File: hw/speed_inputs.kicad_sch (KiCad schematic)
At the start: 21 parts, among them U701 TLV3201

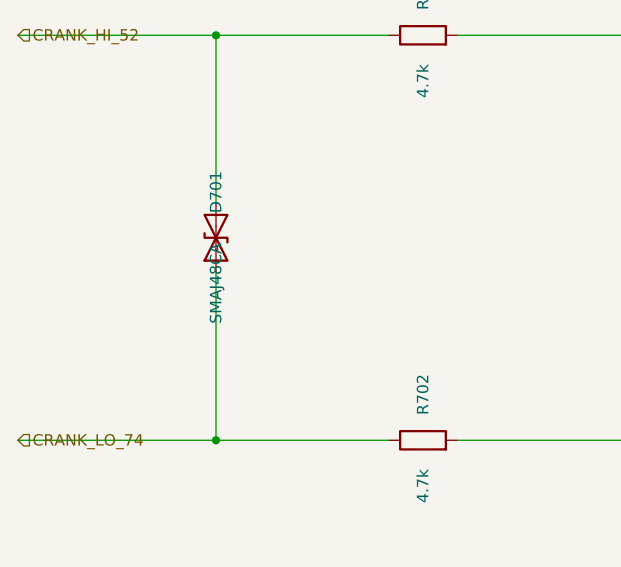
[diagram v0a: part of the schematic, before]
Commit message: Choose the diodes; the boost VDD clamp was 10 V over its pin rating
Part numbers for 27 diodes, each against a retrieved datasheet, applied
through one table (schlib.CHOSEN) keyed by symbol and class value, so
the class stays on the part as a field:
  VS-16EDH02HM3 x7   injector recirculation / blocking / freewheel
  VS-2EMH02HM3       boost diode
  VS-1EMH02HM3 x8    bootstrap and relay flyback
  VS-3ECH02HM3       metering freewheel
  SS20PH102HM3       negative-clamp backstop Schottky
  SMCJ43CA-HM3, SMAJ48CA-HE3, BZX84-C12-Q x2, BZX84-C13-Q, BZG03C36-HM3

The TPS40210 VDD clamp had been checked as an ideal 43.0 V source
behind 47 ohm. The real part in that class (40-46 V, +0.12 %/K, 45 ohm)
puts 61.9 V on a 52 V pin at 125 C, and its 40 V minimum conducts on
the load dump it was chosen to avoid. Now 220 ohm -- which the chosen
switch's gate charge allows -- and a 36 V zener: 46.6 V worst case with
tolerance, tempco and impedance, 33 mA on the dump. 39 V was tried
first; the transient_clamp rail table rejected it at 1.05x. The old
design stays as a pinned check.

TO-277A and SOT-23 zeners put the cathode on pad 3. gen_footprints.py
derives renumbered copies into lib/ecu25kva.pretty (new fp-lib-table).
The GATE_KILL zener, footprinted in the previous commit with the stock
SOT-23, had been reversed.

Left open as LOWV-CLAMP: the 15 zeners at 3.0 and 3.3 V. At tens of uA
a sub-5 V zener's knee is soft -- the datasheet allows 10 uA at 1 V --
and the model's sharp-knee zener hides it.

24/24 sim blocks, netlist gate passing, 74 of 297 parts with footprints.
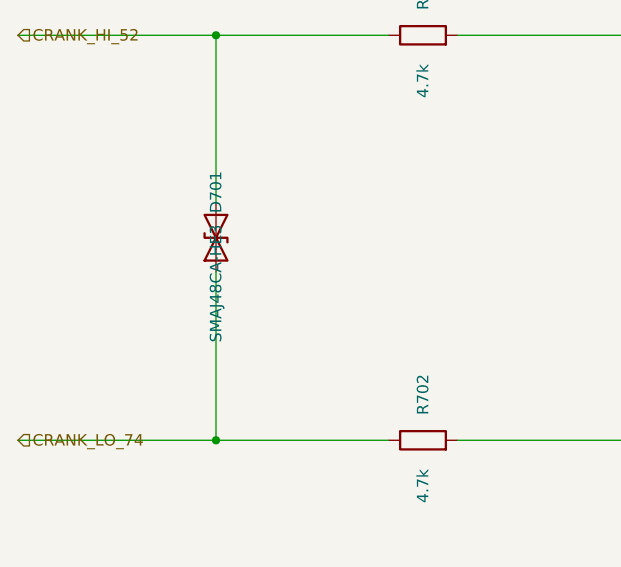
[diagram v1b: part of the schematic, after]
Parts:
- D701: value SMAJ48CA -> SMAJ48CA-HE3; footprint (none) -> Diode_SMD:D_SMA; Chosen (none) -> Vishay TransZorb, 48 V standoff, VBR 53.3-58.9 V, 400 W, AE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; Class (none) -> SMAJ48CA; MPN (none) -> SMAJ48CA-HE3
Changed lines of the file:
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@@
       (effects (font (size 1.27 1.27)))
     )
-    (property "Value" "SMAJ48CA" (id 1) (at 62.0 97.58 0)
+    (property "Value" "SMAJ48CA-HE3" (id 1) (at 62.0 97.58 0)
       (effects (font (size 1.27 1.27)))
     )
-    (property "Footprint" "" (id 2) (at 62.0 92.5 0)
+    (property "Footprint" "Diode_SMD:D_SMA" (id 2) (at 62.0 92.5 0)
       (effects (font (size 1.27 1.27)) hide)
     )
@@
       (effects (font (size 1.27 1.27)) hide)
     )
-    (property "Tag" "VR-CLAMP" (id 4) (at 62.0 92.5 0)
+    (property "MPN" "SMAJ48CA-HE3" (id 4) (at 62.0 92.5 0)
       (effects (font (size 1.27 1.27)) hide)
     )
-    (property "Note" "Bidirectional, across the pair. Standoff has to clear the signal itself: VR amplitude is proportional to speed, about 20 V peak at 1500 rpm, so a part that clamps at 24 V would clip a runaway engine's own crank signal -- the one time the ECU most needs to keep counting teeth. 48 V clears 3600 rpm." (id 5) (at 62.0 92.5 0)
+    (property "Class" "SMAJ48CA" (id 5) (at 62.0 92.5 0)
       (effects (font (size 1.27 1.27)) hide)
     )
+    (property "Chosen" "Vishay TransZorb, 48 V standoff, VBR 53.3-58.9 V, 400 W, AEC-Q101" (id 6) (at 62.0 92.5 0)
+      (effects (font (size 1.27 1.27)) hide)
+    )
+    (property "Tag" "VR-CLAMP" (id 7) (at 62.0 92.5 0)
+      (effects (font (size 1.27 1.27)) hide)
+    )
+    (property "Note" "Bidirectional, across the pair. Standoff has to clear the signal itself: VR amplitude is proportional to speed, about 20 V peak at 1500 rpm, so a part that clamps at 24 V would clip a runaway engine's own crank signal -- the one time the ECU most needs to keep counting teeth. 48 V clears 3600 rpm." (id 8) (at 62.0 92.5 0)
+      (effects (font (size 1.27 1.27)) hide)
+    )

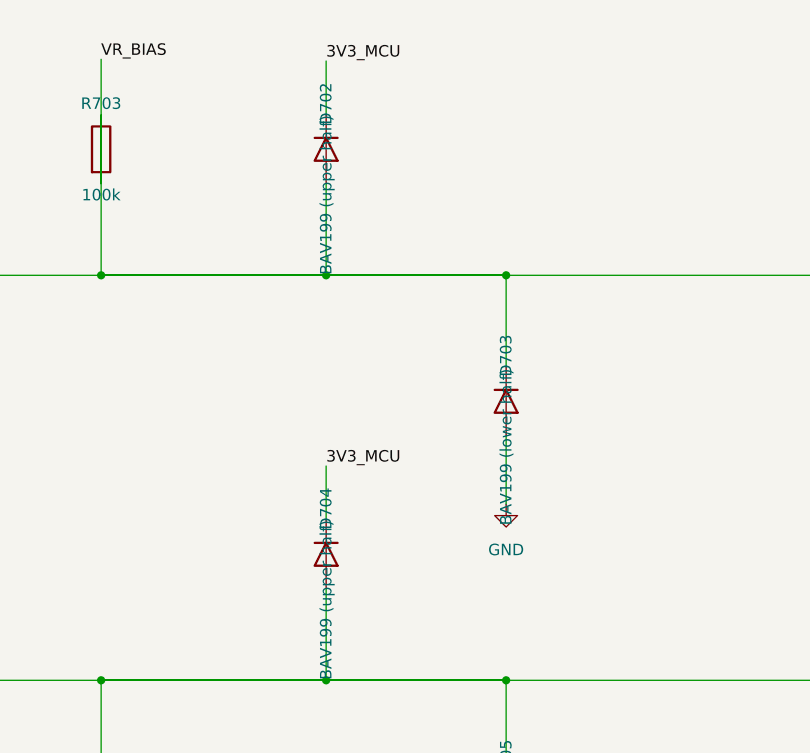
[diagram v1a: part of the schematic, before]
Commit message: Package every resistor and capacitor from the voltage across it
hw/assign_passives.py sizes all 188 chip R and C from a per-net table
of continuous and peak voltage (73.3 V pulse 2a, 104 V boost, bootstrap
domains riding on the bank nodes), against Vishay CRCW e3 resistor
ratings (Umax with 1.09x margin, power derated to 0.588x at a 105 C
board) and KEMET's automotive X7R waterfall (parsed by x-coordinate;
the text layout misreads its columns). schlib.place() applies the map
by ref and value; check_netlist fails on any unpackaged R or C.

Found along the way:
- 4.7 uF at 100 V is not in automotive X7R. The EMI filter C1, buck
  input and boost input are now 2 x 2.2 uF 100 V 1210; emi_filter.cir
  models the pair and its cold corner was re-pinned (0.6 dB worse).
- The twelve 470 ohm gate pulldowns need 2010: 0.31 W each at 100%
  duty. Recorded; 1k may now be possible against the real Crss.
- Local labels at 180 degrees were justified in the wrong frame on
  every sheet -- the bug fixed for hierarchical labels earlier -- so
  their text sat across their own wire. Fixed in schlib.label().

Internal nodes whose voltage matters now carry names (FB_BOOST_MID,
CAN1_SPLIT, ...); auto-names like Net-(R407-Pad2) move when parts are
added ahead of them.

24/24 sim blocks, netlist gate passing, 264 of 302 parts footprinted.
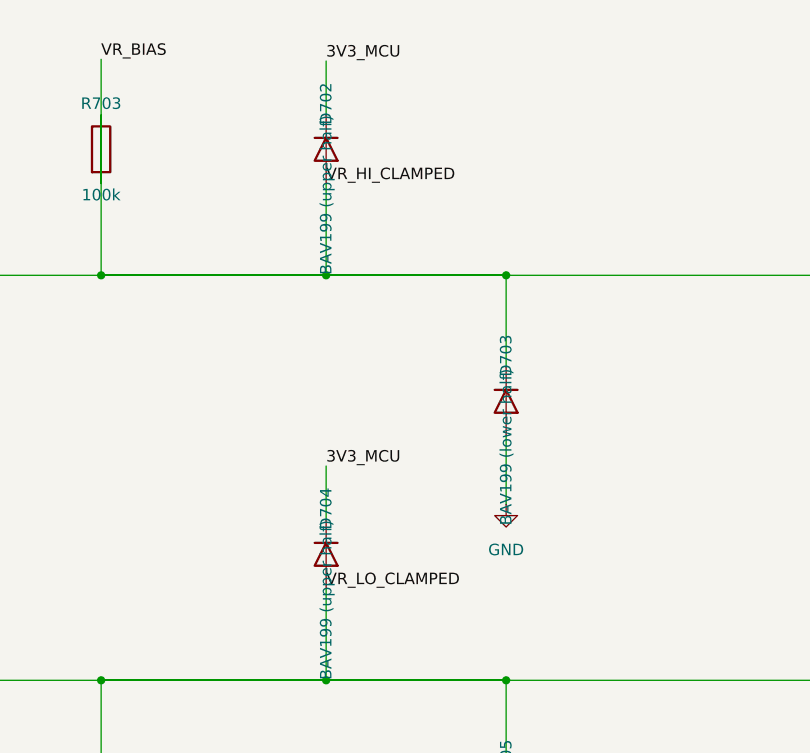
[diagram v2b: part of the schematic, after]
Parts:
- C701, C702, C703, C705: footprint (none) -> Capacitor_SMD:C_0603_1608Metric
- C704: footprint (none) -> Capacitor_SMD:C_0805_2012Metric
- R701, R702, R703, R704, R705, R706, R707, R708, R709: footprint (none) -> Resistor_SMD:R_0603_1608Metric
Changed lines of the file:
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@@
       (effects (font (size 1.27 1.27)))
     )
-    (property "Footprint" "" (id 2) (at 85.0 70.0 0)
+    (property "Footprint" "Resistor_SMD:R_0603_1608Metric" (id 2) (at 85.0 70.0 0)
       (effects (font (size 1.27 1.27)) hide)
     )
@@
       (effects (font (size 1.27 1.27)))
     )
-    (property "Footprint" "" (id 2) (at 110.0 88.0 0)
+    (property "Footprint" "Capacitor_SMD:C_0603_1608Metric" (id 2) (at 110.0 88.0 0)
       (effects (font (size 1.27 1.27)) hide)
     )
@@
   (wire (pts (xy 155.0 70.0) (xy 155.0 59.81))
     (stroke (width 0) (type default))
+  )
+  (label "VR_HI_CLAMPED" (at 155.0 59.81 0)
+    (effects (font (size 1.27 1.27)) (justify left bottom))
   )
   (wire (pts (xy 155.0 52.19) (xy 155.0 46.19))
@@
       (effects (font (size 1.27 1.27)))
     )
-    (property "Footprint" "" (id 2) (at 85.0 115.0 0)
+    (property "Footprint" "Resistor_SMD:R_0603_1608Metric" (id 2) (at 85.0 115.0 0)
       (effects (font (size 1.27 1.27)) hide)
     )
@@
       (effects (font (size 1.27 1.27)))
     )
-    (property "Footprint" "" (id 2) (at 110.0 133.0 0)
+    (property "Footprint" "Capacitor_SMD:C_0603_1608Metric" (id 2) (at 110.0 133.0 0)
       (effects (font (size 1.27 1.27)) hide)
     )
@@
   (wire (pts (xy 155.0 115.0) (xy 155.0 104.81))
     (stroke (width 0) (type default))
+  )
+  (label "VR_LO_CLAMPED" (at 155.0 104.81 0)
+    (effects (font (size 1.27 1.27)) (justify left bottom))
   )
   (wire (pts (xy 155.0 97.19) (xy 155.0 91.19))
@@
       (effects (font (size 1.27 1.27)))
     )
-    (property "Footprint" "" (id 2) (at 130.0 56.0 0)
+    (property "Footprint" "Resistor_SMD:R_0603_1608Metric" (id 2) (at 130.0 56.0 0)
       (effects (font (size 1.27 1.27)) hide)
     )
@@
       (effects (font (size 1.27 1.27)))
     )
-    (property "Footprint" "" (id 2) (at 130.0 129.0 0)
+    (property "Footprint" "Resistor_SMD:R_0603_1608Metric" (id 2) (at 130.0 129.0 0)
       (effects (font (size 1.27 1.27)) hide)
     )
@@
       (effects (font (size 1.27 1.27)))
     )
-    (property "Footprint" "" (id 2) (at 250.0 48.0 0)
+    (property "Footprint" "Resistor_SMD:R_0603_1608Metric" (id 2) (at 250.0 48.0 0)
       (effects (font (size 1.27 1.27)) hide)
     )
@@
       (effects (font (size 1.27 1.27)))
     )
-    (property "Footprint" "" (id 2) (at 300.0 110.0 0)
+    (property "Footprint" "Capacitor_SMD:C_0603_1608Metric" (id 2) (at 300.0 110.0 0)
       (effects (font (size 1.27 1.27)) hide)
     )
@@
       (effects (font (size 1.27 1.27)))
     )
-    (property "Footprint" "" (id 2) (at 60.0 181.0 0)
+    (property "Footprint" "Resistor_SMD:R_0603_1608Metric" (id 2) (at 60.0 181.0 0)
       (effects (font (size 1.27 1.27)) hide)
     )
@@
       (effects (font (size 1.27 1.27)))
     )
-    (property "Footprint" "" (id 2) (at 60.0 203.0 0)
+    (property "Footprint" "Resistor_SMD:R_0603_1608Metric" (id 2) (at 60.0 203.0 0)
       (effects (font (size 1.27 1.27)) hide)
     )
@@
       (effects (font (size 1.27 1.27)))
     )
-    (property "Footprint" "" (id 2) (at 85.0 209.0 0)
+    (property "Footprint" "Capacitor_SMD:C_0805_2012Metric" (id 2) (at 85.0 209.0 0)
       (effects (font (size 1.27 1.27)) hide)
     )
@@
       (effects (font (size 1.27 1.27)))
     )
-    (property "Footprint" "" (id 2) (at 70.0 250.0 0)
+    (property "Footprint" "Resistor_SMD:R_0603_1608Metric" (id 2) (at 70.0 250.0 0)
       (effects (font (size 1.27 1.27)) hide)
     )
@@
       (effects (font (size 1.27 1.27)))
     )
-    (property "Footprint" "" (id 2) (at 120.0 268.0 0)
+    (property "Footprint" "Resistor_SMD:R_0603_1608Metric" (id 2) (at 120.0 268.0 0)
       (effects (font (size 1.27 1.27)) hide)
     )
@@
       (effects (font (size 1.27 1.27)))
     )
-    (property "Footprint" "" (id 2) (at 145.0 268.0 0)
-      (effects (font (size 1.27 1.27)) hide)
-    )
+    (property "Footprint" "Capacitor_SMD:C_0603_1608Metric" (id 2) (at 145.0 268.0 0)
+      (effects (font (size 1.27 1.27)) hide)
+    )

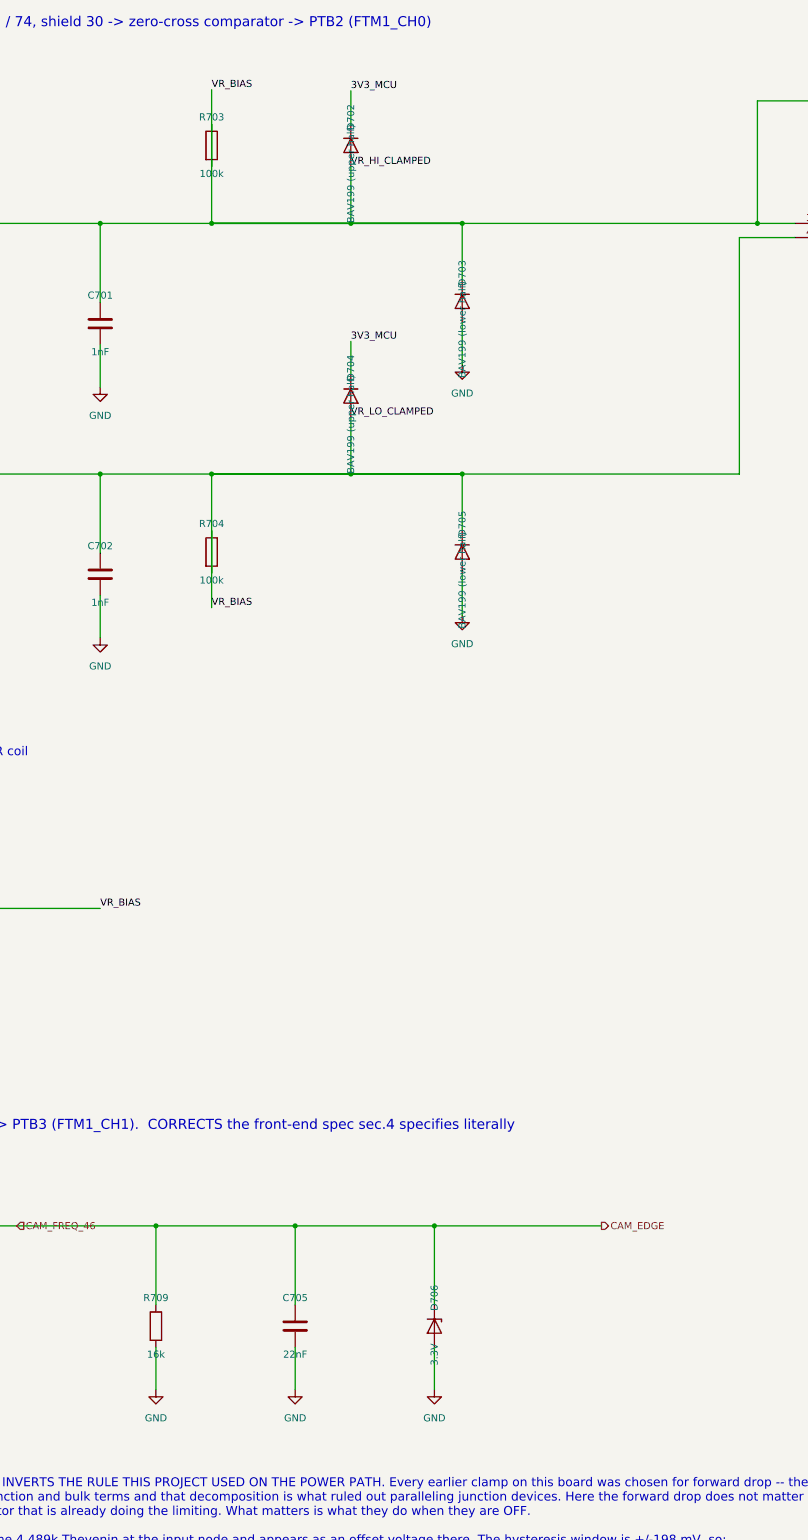
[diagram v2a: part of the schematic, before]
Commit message: Replace the analog-input zeners with BAV199-Q rail clamps
LOWV-CLAMP, analog half. The ten 3.3 V zeners on the sensor and cam
inputs leaked at signal level (the datasheet allows 5 uA at 1 V); they
are now BAV199-Q (80 nA max at 150 C, AEC-Q101) to 3V3_MCU and ground,
drawn as one 3-pin part so each pair is one package. The speed input's
split BAV199 halves and the power-input sense clamp use the same part.

A rail clamp needs something the zener did not: the BAV199's upper
diode is high-Vf, so on a 40 V harness short the MCU pad's ESD diode
would take most of the fault current, over the +/-3 mA injection
limit. Each clamped channel now has 1k between clamp and pad: 0.40 mA
injected. sensor_ratiometric and cam_frontend model the pair, the 1k
and the pad diode, and check the injection current.

The new models also showed the old zener loading the cam signal by
84 mV at a 5.25 V rail -- pinned by the old check as the expected
value. Re-pinned to the divider's own 3.231 V.

The discrete inputs stay open: they clamp continuously, which neither
a rail clamp nor an LM4040-class reference (35 uA bias below
breakdown) can do within the pin's ratings.

24/24 sim blocks, netlist gate passing, 197 R/C packaged.
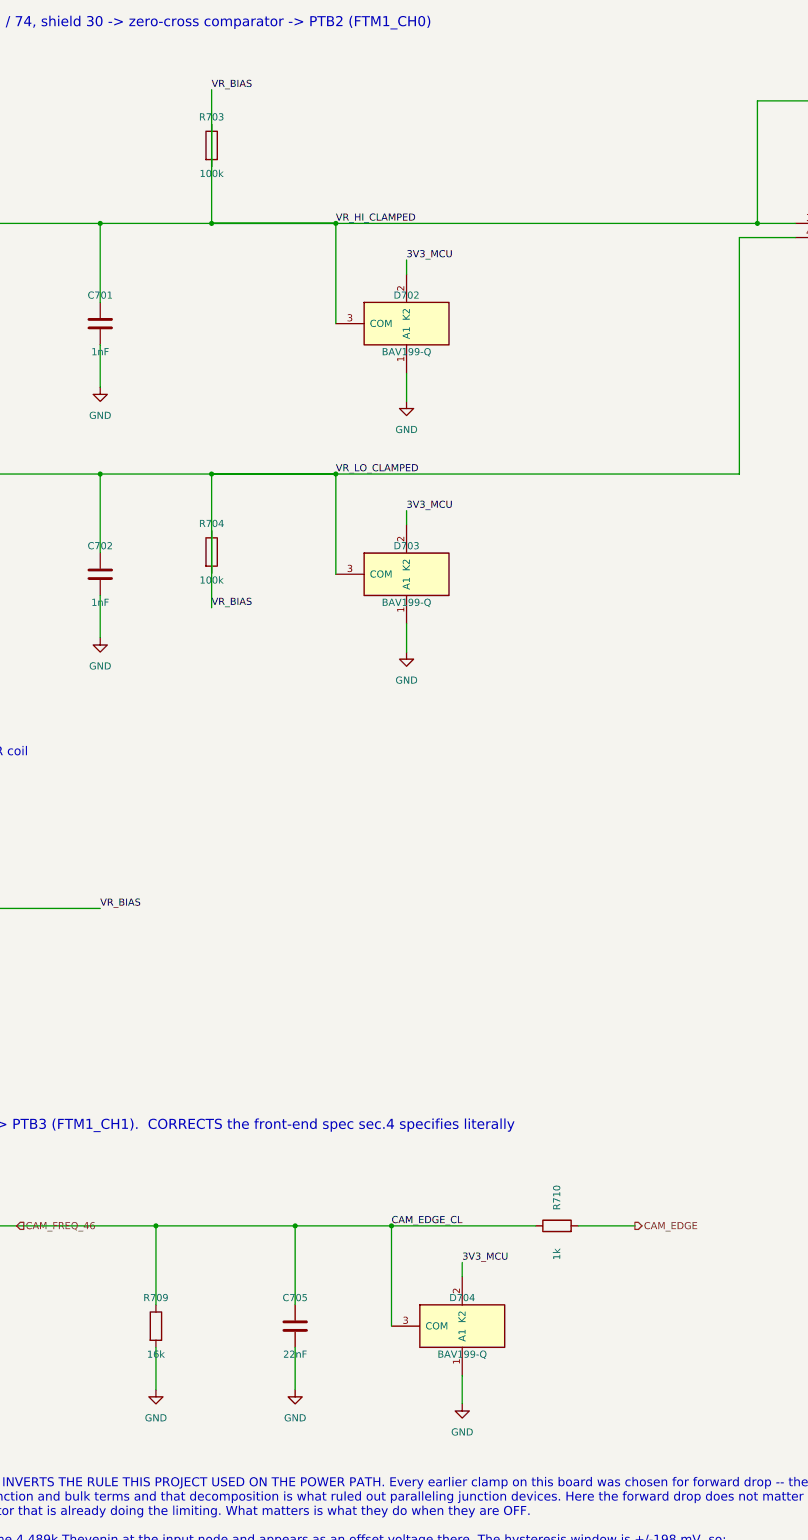
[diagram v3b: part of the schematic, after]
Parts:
- removed D702, D704: BAV199 (upper half), symbol Device:D
- removed D703, D705: BAV199 (lower half), symbol Device:D
- removed D706: 3.3V, symbol Device:D_Zener
- added D702, D703, D704: BAV199-Q, Package_TO_SOT_SMD:SOT-23, symbol ecu25kva:BAV199
- added R710: 1k, Resistor_SMD:R_2512_6332Metric, symbol Device:R
- R708, R709: footprint Resistor_SMD:R_0603_1608Metric -> Resistor_SMD:R_0805_2012Metric
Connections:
- net 3V3_MCU: now also D702.2 (K2), D703.2 (K2), D704.2 (K2)
- net CAM_EDGE: now also R710.2; no longer C705.1, R708.2, R709.1
- net GND: now also D702.1 (A1), D703.1 (A1), D704.1 (A1)
- net VR_BIAS: now also D702.3 (COM), D703.3 (COM)
- new net CAM_FREQ_46: C705.1, D704.3 (COM), R708.2, R709.1, R710.1
